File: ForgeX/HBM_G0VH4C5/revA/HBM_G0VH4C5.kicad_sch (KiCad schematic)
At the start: 34 parts, among them J1 Conn_02x05_Odd_Even, J2 Screw_Terminal_01x03, Q1 STF24N60M2, Q2 STF24N60M2, U1 INA199xxDCK, U3 L6388ED, U7 AMS1117-3.3

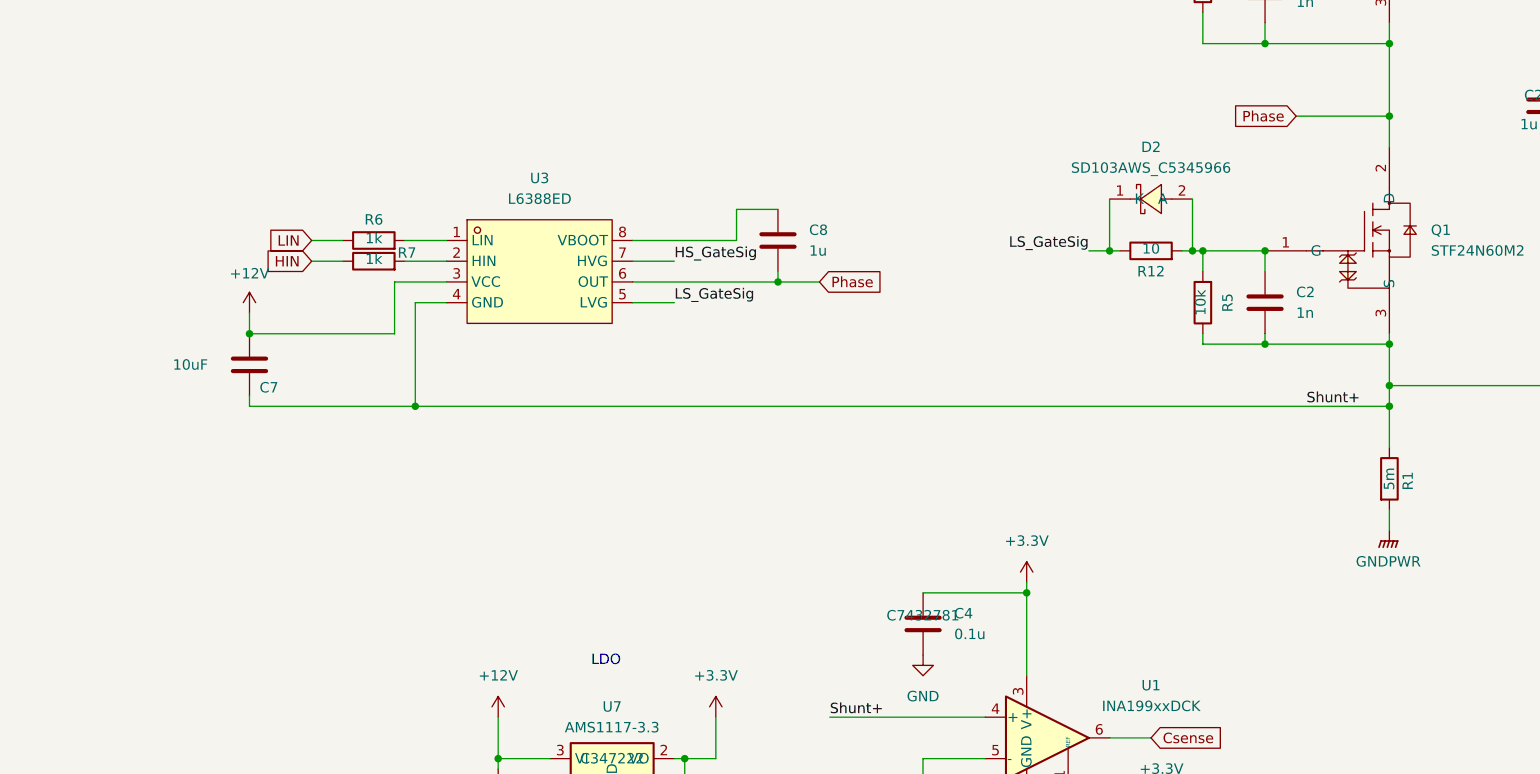
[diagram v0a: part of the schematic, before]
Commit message: BlackDev Fini & HBM mod
Finalized blackDev, HBM with (RC) ground coupling, LVP swapping RS422 to RS485 and processing card interface modifications
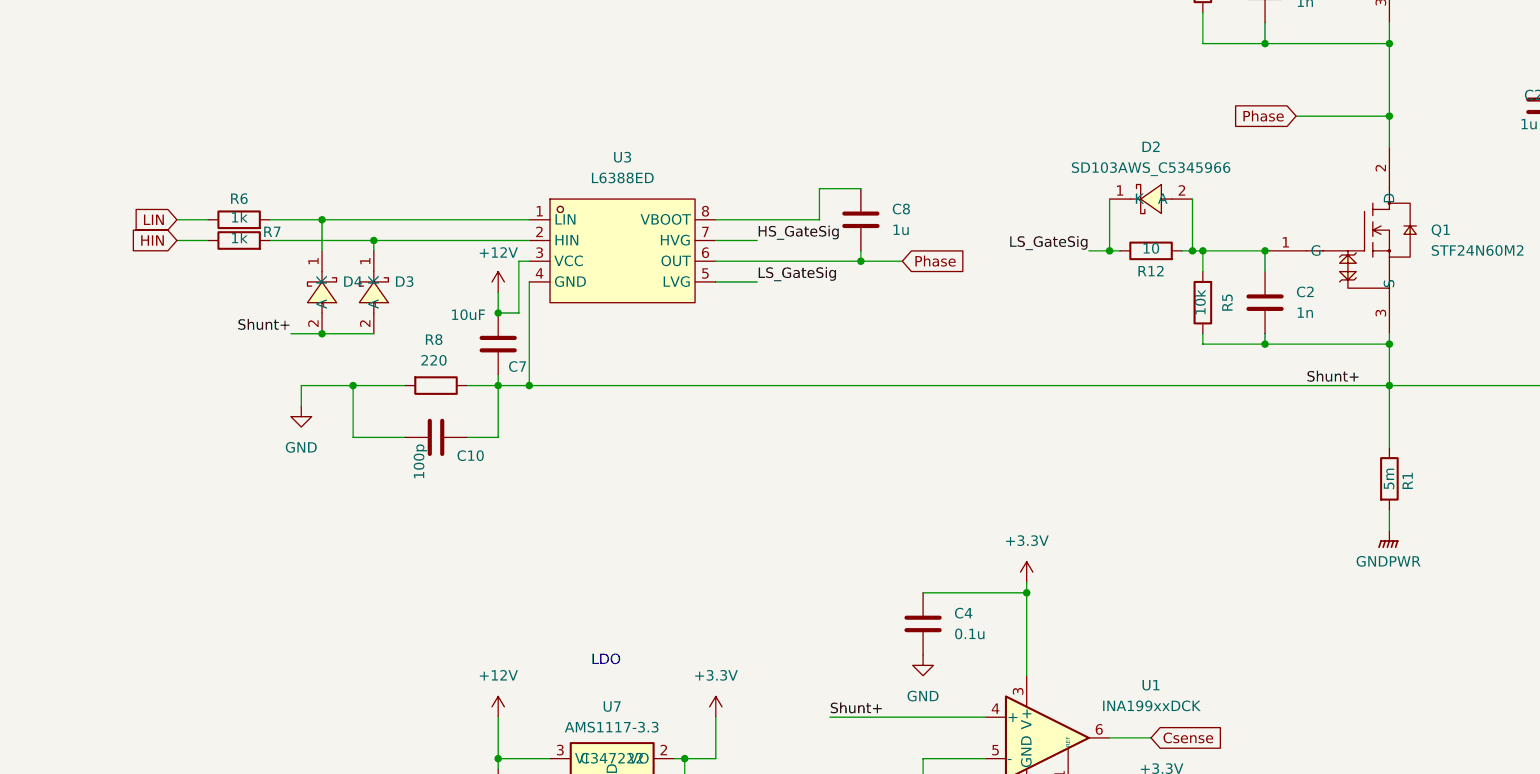
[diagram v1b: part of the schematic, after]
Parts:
- added C10: 100p, Capacitor_SMD:C_1206_3216Metric_Pad1.33x1.80mm_HandSolder, symbol Device:C
- added D3, D4: SD103AWS_C5345966, EasyEDA:SOD-323_L1.7-W1.3-LS2.5-RD, symbol EasyEDA:SD103AWS_C5345966
- added R8: 220, Resistor_SMD:R_1206_3216Metric_Pad1.30x1.75mm_HandSolder, symbol Device:R
- C9: footprint Capacitor_SMD:C_1206_3216Metric_Pad1.33x1.80mm_HandSolder -> Capacitor_SMD:C_0603_1608Metric_Pad1.08x0.95mm_HandSolder
- R26: footprint Resistor_SMD:R_1206_3216Metric_Pad1.30x1.75mm_HandSolder -> Resistor_SMD:R_0603_1608Metric_Pad0.98x0.95mm_HandSolder
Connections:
- net GND: now also C10.2, R8.2
- net Shunt+: now also C10.1, D3.2 (A), D4.2 (A), R8.1
- net at R6.2, U3.1 (LIN): now also D4.1 (K)
- net at R7.2, U3.2 (HIN): now also D3.1 (K)
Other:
- moved on the sheet: C7, C8, R6, R7, U3
